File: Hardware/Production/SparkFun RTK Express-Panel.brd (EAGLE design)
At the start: 219.3 x 141.9 mm, 495 parts, among them J13 Internal, J16 microSD, J17 Qwiic Right Angle, J19 External, J21 USB Female Type C Connector, J24 USB Female Type C Connector, J3 USB Female Type C Connector, J31 microSD, J33 Qwiic Right Angle, J34 Internal, J39 External, J4 External, J40 USB Female Type C Connector, J43 USB Female Type C Connector, J5 USB Female Type C Connector, J50 microSD, J52 Qwiic Right Angle, J53 Internal, Q1 SIL2308-TP, Q2 MBT3904DW1T1, Q3 MBT3904DW1T1, Q4 SIL2308-TP, Q5 MBT3904DW1T1, Q6 SIL2308-TP, U1 74HC4052D, U10 MCP73833, U11 CH340C, U12 MAX17048, U13 LIS2DH12, U14 STLQ015-3.3V, U15 MCP73833, U16 74HC4052D, U17 LIS2DH12, U18 ESP-WROOM-3232D-NARROW, U19 AP2112K-3.3, U2 AP2112K-3.3, U20 U-BLOX_ZED-F9P, U21 CH340C, U22 MAX17048, U23 STLQ015-3.3V, U24 MCP73833, U25 74HC4052D, U26 LIS2DH12, U27 ESP-WROOM-3232D-NARROW, U3 U-BLOX_ZED-F9P, U4 STLQ015-3.3V, U5 ESP-WROOM-3232D-NARROW, U6 CH340C, U7 MAX17048, U8 AP2112K-3.3, U9 U-BLOX_ZED-F9P

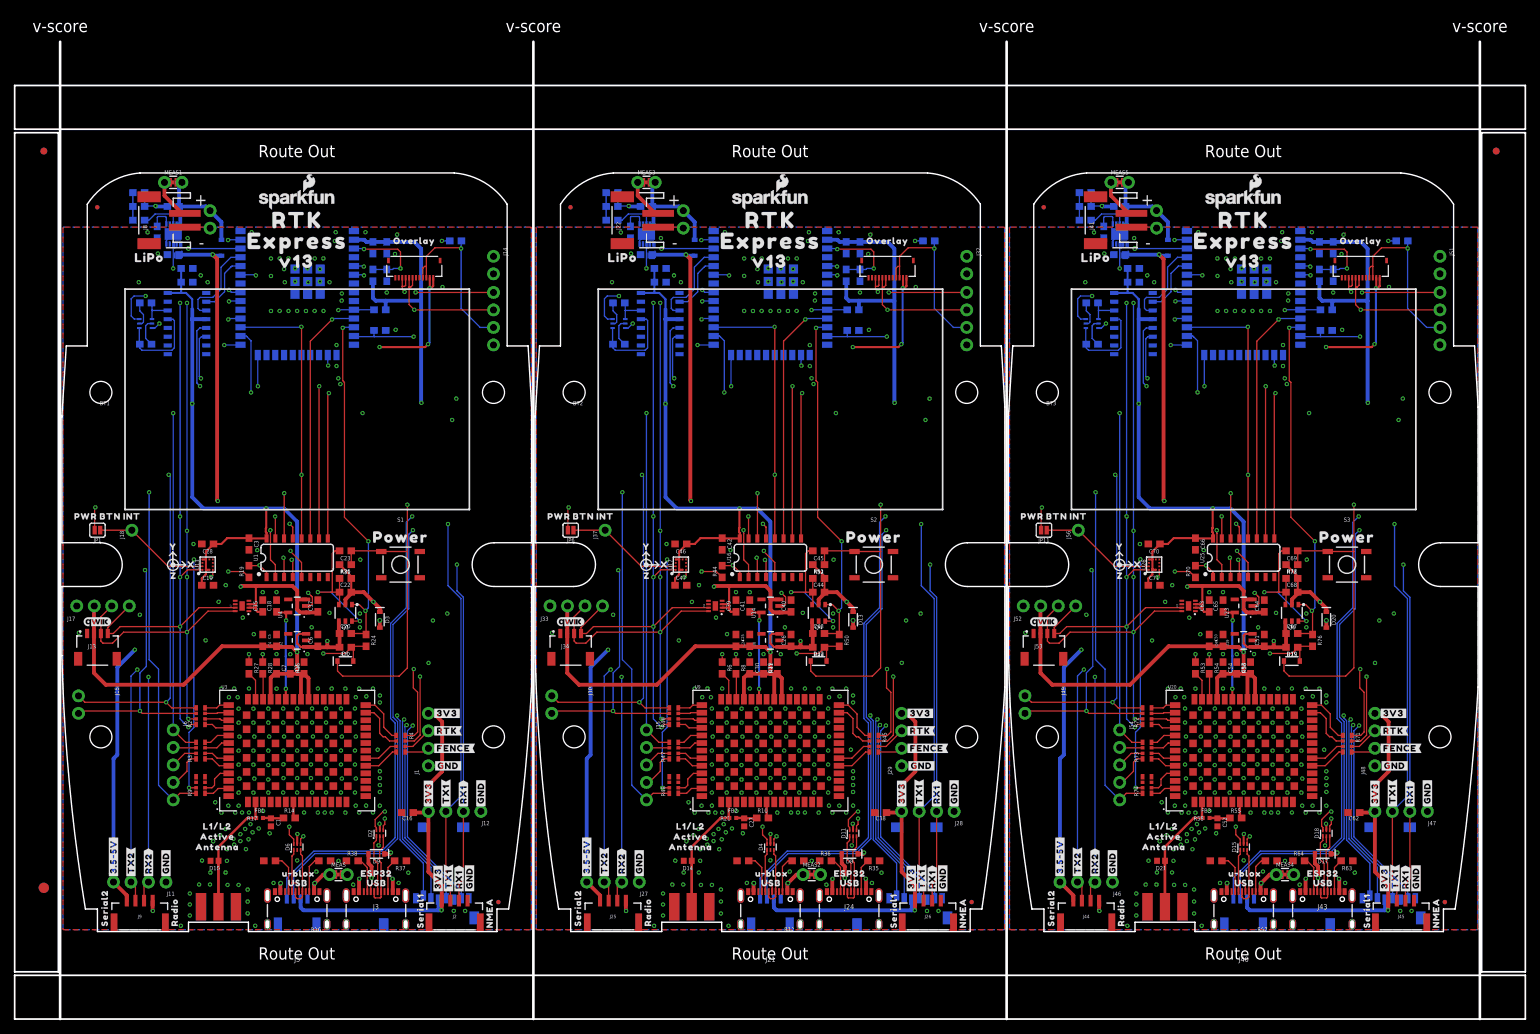
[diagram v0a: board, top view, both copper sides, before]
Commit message: Remove post mux opto isolation. Create v10 panel.
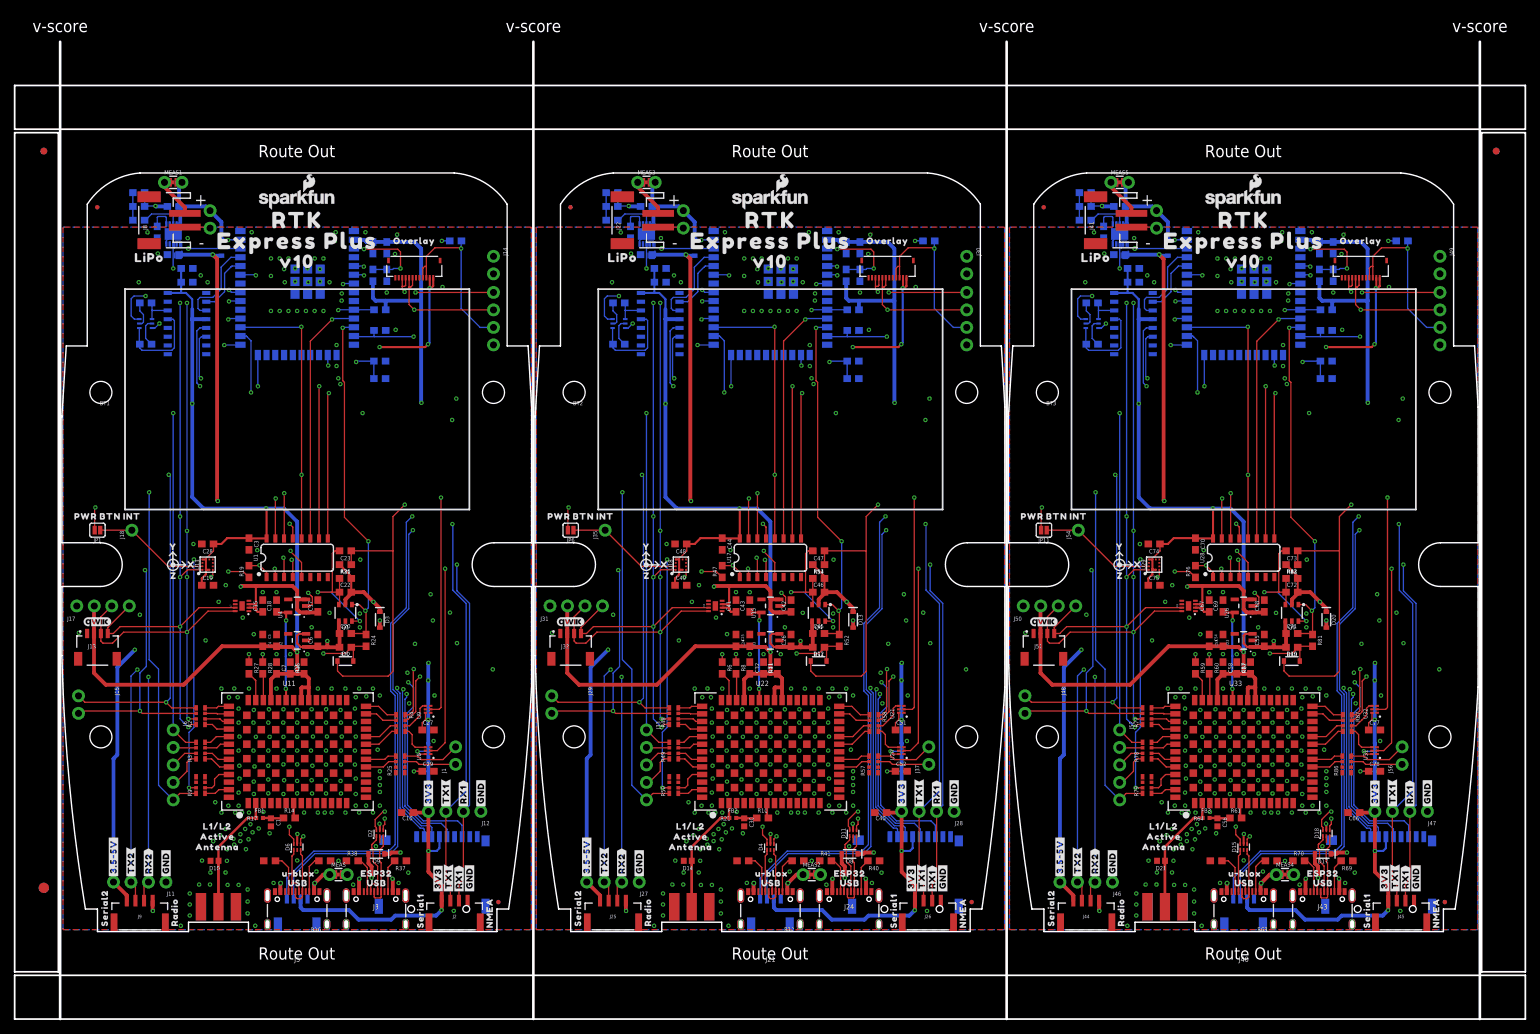
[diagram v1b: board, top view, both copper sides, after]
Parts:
- removed S1, S2, S3: Power, SparkFun-Switches:TACTILE_SWITCH_SMD_5.2MM
- removed U$181: (no value), output:PWR_BTN1
- removed U$182: (no value), output:OVERLAY0
- removed U$183: (no value), output:L1#L20
- removed U$184: (no value), output:ACTIVE1
- removed U$185: (no value), output:ANTENNA2
- removed U$186: (no value), output:V130
- added C73, C74, C76, C77, C78: 0.1uF, SparkFun-Capacitors:0603
- added C75: 10uF, SparkFun-Capacitors:0603
- added R79, R86, R87: 33, SparkFun-Resistors:1206_RA
- added R80, R82: 100k, SparkFun-Resistors:0603
- added R81: 300k, SparkFun-Resistors:0603
- added R83, R84: 10k, SparkFun-Resistors:0603
- added R85: 3.3k, SparkFun-Resistors:0603
- added U28: 74HC4052D, SparkFun-IC-Logic:SO16
- added U29: LIS2DH12, SparkFun-Sensors:LGA-12-LISDH12
- added U30: ESP-WROOM-3232D-NARROW, SparkFun-RF:ESP-WROOM-32D-NARROW
- added U31, U32: NC7SZ14-D, SparkFun-IC-Amplifiers:SIP6
- added U33: U-BLOX_ZED_F9R, SparkFun-GPS:UBLOX_ZED_F9R
- C27, C52: value 47pF -> 0.1uF; device SparkFun-Capacitors:0402 -> SparkFun-Capacitors:0603
- C29, C40, C41, C51, C64: value 1.0uF -> 0.1uF
- C30: value 0.1uF -> 47pF; device SparkFun-Capacitors:0603 -> SparkFun-Capacitors:0402
- C31, C55: value 4.7uF -> 1.0uF
- C32: value 4.7uF -> 0.1uF
- C33: value 10uF -> 4.7uF
- C34, C59, C60: value 0.1uF -> 4.7uF
- C35, C39, C45: value 0.1uF -> 10uF
- C37, C47, C67: value 10uF -> 0.1uF
- C42, C68, C69: value 0.1uF -> 1.0uF
- C43, C57: value 10uF -> 1.0uF
- C49, C65: value 1.0uF -> 10uF
- C56: value 4.7uF -> 47pF; device SparkFun-Capacitors:0603 -> SparkFun-Capacitors:0402
- J1, J29, J48: device SparkFun-Connectors:1X04_NO_SILK -> SparkFun-Connectors:1X02_NO_SILK
- J16: value microSD -> MICRO-SD-PUSH-PUSH-EXT-PIN; device SparkFun-Connectors:MICRO-SD-SOCKET -> SparkFun-Connectors:MICROSD-EXTERNALPIN
- J31, J50: value microSD -> Qwiic Right Angle; device SparkFun-Connectors:MICRO-SD-SOCKET -> SparkFun-Connectors:1X04_NO_SILK
- J32, J51: value (none) -> Internal; device SparkFun-Connectors:1X02_NO_SILK -> SparkFun-Connectors:JST04_1MM_RA
- J33, J52: value Qwiic Right Angle -> (none); device SparkFun-Connectors:1X04_NO_SILK -> SparkFun-Connectors:1X05_NO_SILK
- J34, J53: value Internal -> (none); device SparkFun-Connectors:JST04_1MM_RA -> SparkFun-Connectors:1X04_NO_SILK
- J35, J54: device SparkFun-Connectors:1X05_NO_SILK -> SparkFun-Connectors:1X01_NO_SILK
- J36, J55: device SparkFun-Connectors:1X04_NO_SILK -> RTK Facet:FPC_12_DOUBLESIDED_BACKFLIP
- J37, J56: device SparkFun-Connectors:1X01_NO_SILK -> SparkFun-Connectors:1X02_NO_SILK
- J38, J57: value (none) -> MICRO-SD-PUSH-PUSH-EXT-PIN; device RTK Facet:FPC_12_DOUBLESIDED_BACKFLIP -> SparkFun-Connectors:MICROSD-EXTERNALPIN
- R25: value 1k -> 33; device SparkFun-Resistors:0603 -> SparkFun-Resistors:1206_RA
- R32, R65: value 100k -> 1k
- R34: value 10k -> 3.3k
- R35: value 5.1k -> 100k
- R36: value 5.1k -> 10k
- R39, R75: value 100k -> 10k
- R40: value 470 -> 5.1k
- R41: value 150k -> 5.1k
- R42: value 0 -> 100k
- R43: value 10k -> 470
- R44: value 1k -> 150k
- R45, R74: value 33 -> 0; device SparkFun-Resistors:1206_RA -> SparkFun-Resistors:0603
- R46: value 33 -> 10k; device SparkFun-Resistors:1206_RA -> SparkFun-Resistors:0603
- R47: value 33 -> 1k; device SparkFun-Resistors:1206_RA -> SparkFun-Resistors:0603
- R49, R77: value 100k -> 33; device SparkFun-Resistors:0603 -> SparkFun-Resistors:1206_RA
- R50: value 300k -> 33; device SparkFun-Resistors:0603 -> SparkFun-Resistors:1206_RA
- R52: value 10k -> 300k
- R53: value 27 -> 100k
- R54: value 27 -> 10k
- R55: value 10 -> 10k
- R56: value 100k -> 3.3k
- R57, R58: value 5.1k -> 33; device SparkFun-Resistors:0603 -> SparkFun-Resistors:1206_RA
- R59: value 1k -> 27
- R60: value 100k -> 27
- R61: value 10k -> 10
- R62: value 10k -> 100k
- R66: value 470 -> 100k
- R67: value 150k -> 10k
- R68: value 0 -> 10k
- R69: value 10k -> 5.1k
- R70: value 1k -> 5.1k
- R71: value 33 -> 100k; device SparkFun-Resistors:1206_RA -> SparkFun-Resistors:0603
- R72: value 33 -> 470; device SparkFun-Resistors:1206_RA -> SparkFun-Resistors:0603
- R73: value 33 -> 150k; device SparkFun-Resistors:1206_RA -> SparkFun-Resistors:0603
- R76: value 300k -> 1k
- R78: value 10k -> 33; device SparkFun-Resistors:0603 -> SparkFun-Resistors:1206_RA
- U$1: device output:#GND#0 -> SparkFun-Aesthetics:QWIIC_4MM
- U$100: device output:RTK0 -> output:#SDA#0
- U$101: device output:#GND#2 -> output:#D_SEL#0
- U$102: device output:#3V3#2 -> SparkFun-Aesthetics:QWIIC_4MM
- U$103: device output:#SCL#1 -> output:#TX_RDY#0
- U$104: device output:#SDA#0 -> output:CHG2
- U$105: device output:#D_SEL#0 -> output:GND3
- U$106: device SparkFun-Aesthetics:QWIIC_4MM -> output:PWR0
- U$107: device output:#TX_RDY#0 -> output:SETUP1
- U$108: device output:POWER0 -> output:X0
- U$109: device output:CHG2 -> output:Y1
- U$110: device output:GND3 -> output:Z2
- U$111: device output:PWR0 -> output:INT0
- U$112: device output:SETUP1 -> output:PWR_BTN1
- U$113: device output:EXPRESS0 -> output:OVERLAY0
- U$114: device output:EXPRESS0 -> output:L1#L20
- U$115: device output:X0 -> output:ACTIVE1
- U$116: device output:Y1 -> output:ANTENNA2
- U$117: device output:Z2 -> output:V100
- U$118: device output:INT0 -> output:V100
- U$119: device output:PWR_BTN1 -> output:EXPRESS_PLUS0
- U$12: device output:#3V3#0 -> output:EXPRESS_PLUS0
- U$120: device output:OVERLAY0 -> output:EXPRESS_PLUS0
- U$121: device output:L1#L20 -> SparkFun-Aesthetics:QWIIC_4MM
- U$122: device output:ACTIVE1 -> output:#RTK#1
- U$123: device output:ANTENNA2 -> SparkFun GPS RTK Surveyor:1553DBK-ENCLOSURE
- U$124: device output:V130 -> output:LIPO0
- U$125: device SparkFun-Aesthetics:QWIIC_4MM -> output:U#BLOX0
- U$126: device output:#3V3#0 -> output:USB1
- U$127: device output:#GND#0 -> output:SERIAL20
- U$128: device output:#RTK#1 -> output:SERIAL10
- U$129: device SparkFun GPS RTK Surveyor:1553DBK-ENCLOSURE -> output:#RX2#2
- U$130: device output:LIPO0 -> output:#TX2#1
- U$131: device output:U#BLOX0 -> output:#RX1#2
- U$132: device output:USB1 -> output:#TX1#1
- U$133: device output:SERIAL20 -> output:#3V3#0
- U$134: device output:SERIAL10 -> output:#GND#0
- U$135: device output:#RX2#2 -> output:#GND#0
- U$136: device output:#TX2#1 -> output:NMEA1
- U$137: device output:#RX1#2 -> output:RADIO0
- U$138: device output:#TX1#1 -> output:##RST##4
- U$139: device output:#3V3#0 -> output:##SAFE##5
- U$140: device output:#GND#0 -> output:#FENCE#3
- U$141: device output:#GND#0 -> output:#3#5#5V#0
- U$142: device output:NMEA1 -> output:#PPS#0
- U$143: device output:RADIO0 -> output:#RX#2
- U$144: device output:##RST##4 -> output:ZED0
- U$145: device output:##SAFE##5 -> output:#TX#1
- U$146: device output:#FENCE#3 -> output:USB1
- U$147: device output:#3#5#5V#0 -> output:ESP320
- U$148: device output:#PPS#0 -> output:#3V3#0
- U$149: device output:#RX#2 -> output:#TX1#1
- U$150: device output:ZED0 -> output:#RX1#2
- U$151: device output:#TX#1 -> output:#GND#0
- U$152: device output:USB1 -> output:MICROSD0
- U$153: device output:ESP320 -> output:#GND#1
- U$154: device output:#3V3#0 -> output:#ESP_RST#0
- U$155: device output:#TX1#1 -> output:RTK0
- U$156: device output:#RX1#2 -> output:RTK0
- U$157: device output:#GND#0 -> output:#GND#2
- U$158: device output:MICROSD0 -> output:#3V3#2
- U$159: device output:#GND#1 -> output:#SCL#1
- U$160: device output:#ESP_RST#0 -> output:#SDA#0
- U$161: device output:RTK0 -> output:#D_SEL#0
- U$162: device output:RTK0 -> SparkFun-Aesthetics:QWIIC_4MM
- U$163: device output:#GND#2 -> output:#TX_RDY#0
- U$164: device output:#3V3#2 -> output:CHG2
- U$165: device output:#SCL#1 -> output:GND3
- U$166: device output:#SDA#0 -> output:PWR0
- U$167: device output:#D_SEL#0 -> output:SETUP1
- U$168: device SparkFun-Aesthetics:QWIIC_4MM -> output:X0
- U$169: device output:#TX_RDY#0 -> output:Y1
- U$170: device output:POWER0 -> output:Z2
- U$171: device output:CHG2 -> output:INT0
- U$172: device output:GND3 -> output:PWR_BTN1
- U$173: device output:PWR0 -> output:OVERLAY0
- U$174: device output:SETUP1 -> output:L1#L20
- U$175: device output:EXPRESS0 -> output:ACTIVE1
- U$176: device output:EXPRESS0 -> output:ANTENNA2
- U$177: device output:X0 -> output:V100
- U$178: device output:Y1 -> output:V100
- U$179: device output:Z2 -> output:EXPRESS_PLUS0
- U$18: device output:V130 -> SparkFun GPS RTK Surveyor:1553DBK-ENCLOSURE
- U$180: device output:INT0 -> output:EXPRESS_PLUS0
- U$19: device output:#GND#0 -> output:LIPO0
- U$2: device SparkFun-Aesthetics:QWIIC_4MM -> output:#RTK#1
- U$20: device output:#RTK#1 -> output:V100
- U$21: device SparkFun GPS RTK Surveyor:1553DBK-ENCLOSURE -> output:V100
- U$22: device output:LIPO0 -> output:EXPRESS_PLUS0
- U$31: device output:POWER0 -> output:USB1
- U$37: device output:#3V3#0 -> output:SERIAL20
- U$44: device output:USB1 -> output:SERIAL10
- U$51: device output:EXPRESS0 -> output:#RX2#2
- U$52: device output:SERIAL20 -> output:#TX2#1
- U$53: device output:EXPRESS0 -> output:#RX1#2
- U$54: device output:SERIAL10 -> output:#TX1#1
- U$57: device output:#RX2#2 -> output:#3V3#0
- U$58: device output:#TX2#1 -> output:#GND#0
- U$59: device output:#RX1#2 -> output:#GND#0
- U$61: device output:#TX1#1 -> output:NMEA1
- U$62: device output:#3V3#0 -> output:RADIO0
- U$63: device output:#GND#0 -> output:##RST##4
- U$64: device output:#GND#0 -> output:##SAFE##5
- U$69: device output:NMEA1 -> output:#FENCE#3
- U$71: device output:RADIO0 -> output:#3#5#5V#0
- U$73: device output:##RST##4 -> output:#PPS#0
- U$75: device output:##SAFE##5 -> output:#RX#2
- U$76: device output:#FENCE#3 -> output:ZED0
- U$77: device output:#3#5#5V#0 -> output:#TX#1
- U$78: device output:#PPS#0 -> output:USB1
- U$79: device output:#RX#2 -> output:ESP320
- U$80: device output:ZED0 -> output:#3V3#0
- U$81: device output:#TX#1 -> output:#TX1#1
- U$89: device output:USB1 -> output:#RX1#2
- U$90: device output:ESP320 -> output:#GND#0
- U$91: device output:#3V3#0 -> output:MICROSD0
- U$92: device output:#TX1#1 -> output:#GND#1
- U$94: device output:#RX1#2 -> output:#ESP_RST#0
- U$95: device output:#GND#0 -> output:RTK0
- U$96: device output:MICROSD0 -> output:RTK0
- U$97: device output:#GND#1 -> output:#GND#2
- U$98: device output:#ESP_RST#0 -> output:#3V3#2
- U$99: device output:RTK0 -> output:#SCL#1
- U11: value CH340C -> U-BLOX_ZED_F9R; device SparkFun-IC-Comms:SO016 -> SparkFun-GPS:UBLOX_ZED_F9R
- U12: value MAX17048 -> CH340C; device SparkFun-IC-Power:DFN-8 -> SparkFun-IC-Comms:SO016
- U14: value STLQ015-3.3V -> MAX17048; device SparkFun-IC-Power:SOT23-5 -> SparkFun-IC-Power:DFN-8
- U15: value MCP73833 -> STLQ015-3.3V; device SparkFun-IC-Power:DFN-10 -> SparkFun-IC-Power:SOT23-5
- U16: value 74HC4052D -> MCP73833; device SparkFun-IC-Logic:SO16 -> SparkFun-IC-Power:DFN-10
- U17: value LIS2DH12 -> 74HC4052D; device SparkFun-Sensors:LGA-12-LISDH12 -> SparkFun-IC-Logic:SO16
- U18: value ESP-WROOM-3232D-NARROW -> LIS2DH12; device SparkFun-RF:ESP-WROOM-32D-NARROW -> SparkFun-Sensors:LGA-12-LISDH12
- U19: value AP2112K-3.3 -> ESP-WROOM-3232D-NARROW; device SparkFun-IC-Power:SOT23-5 -> SparkFun-RF:ESP-WROOM-32D-NARROW
- U20, U9: value U-BLOX_ZED-F9P -> NC7SZ14-D; device SparkFun-GPS:ZED-F9P -> SparkFun-IC-Amplifiers:SIP6
- U21: value CH340C -> NC7SZ14-D; device SparkFun-IC-Comms:SO016 -> SparkFun-IC-Amplifiers:SIP6
- U22: value MAX17048 -> U-BLOX_ZED_F9R; device SparkFun-IC-Power:DFN-8 -> SparkFun-GPS:UBLOX_ZED_F9R
- U23: value STLQ015-3.3V -> AP2112K-3.3
- U24: value MCP73833 -> CH340C; device SparkFun-IC-Power:DFN-10 -> SparkFun-IC-Comms:SO016
- U25: value 74HC4052D -> MAX17048; device SparkFun-IC-Logic:SO16 -> SparkFun-IC-Power:DFN-8
- U26: value LIS2DH12 -> STLQ015-3.3V; device SparkFun-Sensors:LGA-12-LISDH12 -> SparkFun-IC-Power:SOT23-5
- U27: value ESP-WROOM-3232D-NARROW -> MCP73833; device SparkFun-RF:ESP-WROOM-32D-NARROW -> SparkFun-IC-Power:DFN-10
- U3: value U-BLOX_ZED-F9P -> AP2112K-3.3; device SparkFun-GPS:ZED-F9P -> SparkFun-IC-Power:SOT23-5
- U8: value AP2112K-3.3 -> NC7SZ14-D; device SparkFun-IC-Power:SOT23-5 -> SparkFun-IC-Amplifiers:SIP6
- moved U$20 111.5 mm to (34.2, 97.3)
- moved R69 104.2 mm to (186.6, 10.3), flipped to the top, turned to 180 degrees
- moved U$51 103.9 mm to (81.3, 7.70), turned to 90 degrees
- moved U$122 103.7 mm to (194.1, 26.8), flipped to the bottom
- moved U$53 102.5 mm to (126.4, 5.51), flipped to the top, turned to 90 degrees
- moved R41 99.9 mm to (110.9, 10.3), flipped to the top
- moved J38 93.0 mm to (122.5, 3.27), flipped to the bottom, turned to 0 degrees
- moved J57 93.0 mm to (191.2, 3.27), flipped to the bottom, turned to 0 degrees
- moved R40 90.4 mm to (117.9, 10.3), flipped to the top, turned to 180 degrees
- moved U$12 90.2 mm to (34.2, 50.3), flipped to the bottom
- moved U$130 90.2 mm to (147.4, 7.70), turned to 90 degrees
- moved U$123 90.2 mm to (171.6, 53.3), turned to 90 degrees
- moved U$95 89.5 mm to (102.9, 103.3), turned to 0 degrees
- moved U$153 89.2 mm to (199.5, 95.4), flipped to the bottom
- moved U$155 88.1 mm to (171.6, 103.3), turned to 0 degrees
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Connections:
- removed net ESP_I3: U27.4
- removed net ESP_I35: U5.7
- removed net ESP_I4: U27.7
- removed net N$14 (its old number): R42.1, U15.8
- removed net N$16 (its old number): R44.1, U18.28
- removed net N$29 (its old number): C68.1, C69.2, Q6.D1, Q6.G2, R77.1
- removed net PPS: R9.P1, U3.53
- removed net PPS1: R48.P1, U9.53
- removed net PPS2: R74.P1, U20.53
- removed net RTK_LV: R4.P3, U3.20
- removed net RTK_LV1: R45.P3, U9.20
- removed net RTK_LV2: R71.P3, U20.20
- new net ESP_3V1: R56.2
- new net ESP_3V2: R85.2
- new net ESP_3V3: R34.2
- new net ESP_I35/DEVICE_SENSE: R33.2, R34.1, U5.7
- new net ESP_I35/DEVICE_SENSE1: R55.2, R56.1, U19.7
- new net ESP_I35/DEVICE_SENSE2: R84.2, R85.1, U30.7
- new net EXT_DIR: U1.15, U9.P2
- new net EXT_DIR1: U17.15, U21.P2
- new net EXT_DIR2: U28.15, U32.P2
- new net EXT_WT: U1.2, U8.P2
- new net EXT_WT1: U17.2, U20.P2
- new net EXT_WT2: U28.2, U31.P2
- new net N$10: Q3.2, R39.2
- new net N$23: R60.2, U33.P39
- new net N$26: R61.2, U33.P7
- new net N$31: R74.1, U27.8
- new net N$33: R76.1, U30.28
- new net N$34: C72.1, C73.2, Q6.D1, Q6.G2, R82.1
- new net N$35: R87.P4, U33.P22
- new net N$36: R87.P3, U33.P23
- new net N$9: Q3.5, R36.2
- new net PPS_LV: R9.P1, U11.P53
- new net PPS_LV1: R50.P1, U22.P53
- new net PPS_LV2: R79.P1, U33.P53
- new net RTK_STAT_LV: R25.P5, U11.P20
- new net RTK_STAT_LV1: R57.P5, U22.P20
- new net RTK_STAT_LV2: R86.P5, U33.P20
- new net ZED_DIR: R4.P6, U9.P4
- new net ZED_DIR1: R58.P6, U21.P4
- new net ZED_DIR2: R87.P6, U32.P4
- new net ZED_WT: R4.P5, U8.P4
- new net ZED_WT1: R58.P5, U20.P4
- new net ZED_WT2: R87.P5, U31.P4
- net 3.3V: now also C27.1, C29.1, J16.4, U11.P33, U11.P34, U11.P38, U8.P6, U9.P6; no longer J1.4, J16.VCC, U3.33, U3.34, U3.38
- net 3.3V1: now also C31.1, C32.2, C35.1, C39.1, C40.1, C44.1, C48.1, C49.1, C51.1, C52.1, J31.2, J32.2, J38.4, R35.2, R42.2, U12.16, U12.4, U17.16, U18.10, U18.3, U18.9, U19.2, U20.P6, U21.P6, U22.P33, U22.P34, U22.P38, U3.5; no longer C29.1, C30.2, C33.1, C34.1, C37.1, C42.1, C46.1, C47.1, J29.4, J31.VCC, J33.2, J34.2, R32.2, R39.2, U11.16, U11.4, U16.16, U17.10, U17.2, U17.3, U17.9, U8.5, U9.33, U9.34, U9.38
- net 3.3V2: now also C58.2, C64.1, C65.1, C74.1, C75.1, C77.1, C78.1, J50.2, J51.2, J57.4, R62.2, R66.2, R71.2, U23.5, U24.16, U24.4, U28.16, U29.10, U29.2, U29.3, U29.9, U30.2, U31.P6, U32.P6, U33.P33, U33.P34, U33.P38; no longer C49.1, C50.2, C58.1, C60.1, C71.1, J48.4, J50.VCC, J52.2, J53.2, R56.2, R60.2, R65.2, U19.5, U20.33, U20.34, U20.38, U21.16, U21.4, U25.16, U26.10, U26.2, U26.3, U26.9, U27.2
- net ANT_VCC1: now also C30.1; no longer C27.1
- net ANT_VCC2: now also C56.1, R61.1; no longer C52.1, R55.1
- net CC10: now also R63.2; no longer R57.2
- net CC11: now also R69.2; no longer R63.2
- net CC12: now also R70.2; no longer R64.2
- net CC7: now also R40.2; no longer R35.2
- net CC8: now also R41.2; no longer R36.2
- net CC9: now also R64.2; no longer R58.2
- net CHG_LED1: now also R43.2, U16.3; no longer R40.2, U15.3
- net CHG_LED2: now also R72.2, U27.3; no longer R66.2, U24.3
- net CHG_LED_RES1: now also J34.2, J36.3, J36.4, R43.1; no longer J36.2, J38.3, J38.4, R40.1
- net CHG_LED_RES2: now also J53.2, J55.3, J55.4, R72.1; no longer J55.2, J57.3, J57.4, R66.1
- net CHG_THERM2: now also R44.2, R45.2, R46.2; no longer R41.2, R42.2, R43.2
- net CHG_THERM3: now also R73.2, R74.2, R75.2; no longer R67.2, R68.2, R69.2
- net D+3: now also U12.5; no longer U11.5
- net D+4: now also R59.1; no longer R53.1
- net D+5: now also U24.5; no longer U21.5
- net D-3: now also U12.6; no longer U11.6
- net D-4: now also R60.1; no longer R54.1
- net D-5: now also U24.6; no longer U21.6
- net ESP32_!DTR1: now also R36.1, U12.13; no longer R33.1, U11.13
- net ESP32_!DTR2: now also R67.1, U24.13; no longer R61.1, U21.13
- net ESP32_!RTS1: now also R39.1, U12.14; no longer R34.1, U11.14
- net ESP32_!RTS2: now also R68.1, U24.14; no longer R62.1, U21.14
- net ESP32_EN1: now also C37.1, J30.1, R35.1, U19.3; no longer C35.1, J32.1, R32.1, U18.3
- net ESP32_EN2: now also C63.1, J49.1, R66.1, U30.3; no longer C59.1, J51.1, R60.1, U27.3
- net ESP32_RXI1: now also U12.2, U19.34; no longer U11.2, U18.34
- net ESP32_RXI2: now also U24.2, U30.34; no longer U21.2, U27.34
- net ESP32_TXO1: now also U12.3, U19.35; no longer U11.3, U18.35
- net ESP32_TXO2: now also U24.3, U30.35; no longer U21.3, U27.35
- net ESP_0/BOOT1: now also U19.25; no longer U18.25
- net ESP_0/BOOT2: now also U30.25; no longer U27.25
- net ESP_1: now also U19.29; no longer U18.29
- net ESP_10: now also U30.9; no longer U27.9
- net ESP_11: now also U30.8; no longer U27.8
- net ESP_13/POWER_CTRL1: now also R51.1, R52.2, U19.16; no longer R49.1, R50.2, U18.16
- net ESP_13/POWER_CTRL2: now also R80.1, R81.2, U30.16; no longer R75.1, R76.2, U27.16
- net ESP_14/SETUP_BUTTON1: now also C50.1, J34.3, J36.7, J36.8, U19.13; no longer C48.1, J36.3, J38.7, J38.8, U18.13
- net ESP_14/SETUP_BUTTON2: now also C76.1, J53.3, J55.7, J55.8, U30.13; no longer C72.1, J55.3, J57.7, J57.8, U27.13
- net ESP_18/SCK: now also J16.5; no longer J16.SCLK
- net ESP_18/SCK1: now also J38.5, U19.30; no longer J31.SCLK, U18.30
- net ESP_18/SCK2: now also J57.5, U30.30; no longer J50.SCLK, U27.30
- net ESP_19/CIPO: now also J16.7; no longer J16.DO/DAT0
- net ESP_19/CIPO1: now also J38.7, U19.31; no longer J31.DO/DAT0, U18.31
- net ESP_19/CIPO2: now also J57.7, U30.31; no longer J50.DO/DAT0, U27.31
- net ESP_2: now also U19.14; no longer U18.14
- net ESP_2/MUX_A1: now also U17.10, U19.24; no longer U16.10, U18.24
- net ESP_2/MUX_A2: now also U28.10, U30.24; no longer U25.10, U27.24
- net ESP_21/SDA: no longer U1.2
- net ESP_21/SDA1: now also J31.3, J32.3, R48.P7, U14.8, U18.4, U19.33; no longer J33.3, J34.3, R46.P7, U12.8, U16.2, U17.4, U18.33
- net ESP_21/SDA2: now also J50.3, J51.3, R77.P7, U25.8, U29.4, U30.33; no longer J52.3, J53.3, R72.P7, U22.8, U25.2, U26.4, U27.33
- net ESP_22/SCL: no longer U1.15
- net ESP_22/SCL1: now also J31.4, J32.4, R48.P8, U14.7, U18.1, U19.36; no longer J33.4, J34.4, R46.P8, U12.7, U16.15, U17.1, U18.36
- net ESP_22/SCL2: now also J50.4, J51.4, R77.P8, U25.7, U29.1, U30.36; no longer J52.4, J53.4, R72.P8, U22.7, U25.15, U26.1, U27.36
- net ESP_23/COPI: now also J16.3; no longer J16.DI/CMD
- net ESP_23/COPI1: now also J38.3, U19.37; no longer J31.DI/CMD, U18.37
- net ESP_23/COPI2: now also J57.3, U30.37; no longer J50.DI/CMD, U27.37
- net ESP_25/SD_!CS!: now also J16.2; no longer J16.CS/DAT3
- net ESP_25/SD_!CS!1: now also J38.2, R42.1, U19.10; no longer J31.CS/DAT3, R39.1, U18.10
- net ESP_25/SD_!CS!2: now also J57.2, R71.1, U30.10; no longer J50.CS/DAT3, R65.1, U27.10
- net ESP_26/DAC1: now also U17.11, U19.11; no longer U16.11, U18.11
- net ESP_26/DAC3: now also U28.11, U30.11; no longer U25.11, U27.11
- net ESP_26/ZED_TX_READY_LV: now also U11.P46; no longer U3.46
- net ESP_26/ZED_TX_READY_LV1: now also R49.P4, U22.P46; no longer R47.P4, U9.46
- net ESP_26/ZED_TX_READY_LV2: now also R78.P4, U33.P46; no longer R73.P4, U20.46
- net ESP_27/FAST_OFF1: now also C45.2, R52.1, U19.12; no longer C43.2, R50.1, U18.12
- net ESP_27/FAST_OFF2: now also C71.2, R81.1, U30.12; no longer C67.2, R76.1, U27.12
- net ESP_3: now also U19.23; no longer U18.23
- net ESP_4: now also U19.9; no longer U18.9
- net ESP_4/ACCEL_INT1: now also J35.1, U18.12; no longer J37.1, U17.12
- net ESP_4/ACCEL_INT2: now also J54.1, U29.12; no longer J56.1, U26.12
- net ESP_4/MUX_B1: now also U17.9, U19.26; no longer U16.9, U18.26
- net ESP_4/MUX_B2: now also U28.9, U30.26; no longer U25.9, U27.26
- net ESP_6: now also U19.8; no longer U18.8
- net ESP_7: now also U30.29; no longer U27.29
- net ESP_8: now also U30.14; no longer U27.14
- net ESP_9: now also U30.23; no longer U27.23
- net ESP_I1: now also U19.4; no longer U18.4
- net ESP_I16/ZED-TXO2: now also J29.1, R48.P5, U17.12, U19.27; no longer J30.1, R46.P5, U16.12, U18.27
- net ESP_I16/ZED-TXO3: now also J48.1, R77.P5, U28.12, U30.27; no longer J49.1, R72.P5, U25.12, U27.27
- net ESP_I2: now also U30.4; no longer U18.7
- net ESP_I34/ZED_TX_READY1: now also J33.1, R49.P5, U19.6; no longer J35.1, R47.P5, U18.6
- net ESP_I34/ZED_TX_READY2: now also J52.1, R78.P5, U30.6; no longer J54.1, R73.P5, U27.6
- net ESP_I39/ADC1: now also U17.4, U19.5; no longer U16.4, U18.5
- net ESP_I39/ADC2: now also U28.4, U30.5; no longer U25.4, U27.5
- net ESP_O17/ZED-RXI2: now also J29.2, R47.2, R48.P6, U17.1; no longer J30.2, R44.2, R46.P6, U16.1
- net ESP_O17/ZED-RXI3: now also J48.2, R76.2, R77.P6, U28.1; no longer J49.2, R70.2, R72.P6, U25.1
- net EXTERNAL_DATA_IN1: now also U17.3; no longer U16.3
- net EXTERNAL_DATA_IN2: now also U28.3; no longer U25.3
- net EXTERNAL_DATA_OUT1: now also U17.13; no longer U16.13
- net EXTERNAL_DATA_OUT2: now also U28.13; no longer U25.13
- net EXTINT_LV: now also U11.P51; no longer U3.51
- net EXTINT_LV1: now also R50.P2, U22.P51; no longer R48.P2, U9.51
- net EXTINT_LV2: now also R79.P2, U33.P51; no longer R74.P2, U20.51
- net FENCE_LV: now also R25.P6, U11.P19; no longer R4.P4, U3.19
- net FENCE_LV1: now also R57.P6, U22.P19; no longer R45.P4, U9.19
- net FENCE_LV2: now also R86.P6, U33.P19; no longer R71.P4, U20.19
- net GND: now also C27.2, C29.2, J16.10, J16.11, J16.12, J16.13, J16.6, R33.1, U11.G1, U11.G10, U11.G11, U11.G12, U11.G13, U11.G14, U11.G15, U11.G16, U11.G17, U11.G18, U11.G19, U11.G2, U11.G20, U11.G21, U11.G22, U11.G23, U11.G24, U11.G25, U11.G26, U11.G27, U11.G28, U11.G29, U11.G3, U11.G30, U11.G31, U11.G32, U11.G33, U11.G34, U11.G35, U11.G36, U11.G37, U11.G38, U11.G39, U11.G4, U11.G40, U11.G41, U11.G42, U11.G43, U11.G44, U11.G45, U11.G46, U11.G47, U11.G48, U11.G5, U11.G6, U11.G7, U11.G8, U11.G9, U11.P1, U11.P12, U11.P14, U11.P3, U11.P32, U11.P37, U11.P41, U11.P48, U8.P3, U9.P3; no longer J1.1, J16.CD1, J16.GND, J16.GND1, J16.GND3, S1.3, U3.1, U3.100, U3.101, U3.102, U3.12, U3.14, U3.3, U3.32, U3.37, U3.41, U3.48, U3.55, U3.56, U3.57, U3.58, U3.59, U3.60, U3.61, U3.62, U3.63, U3.64, U3.65, U3.66, U3.67, U3.68, U3.69, U3.70, U3.71, U3.72, U3.73, U3.74, U3.75, U3.76, U3.77, U3.78, U3.79, U3.80, U3.81, U3.82, U3.83, U3.84, U3.85, U3.86, U3.87, U3.88, U3.89, U3.90, U3.91, U3.92, U3.93, U3.94, U3.95, U3.96, U3.97, U3.98, U3.99
- net GND1: now also C30.2, C32.1, C43.2, C44.2, C49.2, C50.2, C51.2, C52.2, J30.2, J31.1, J32.1, J36.11, J36.12, J38.10, J38.13, J38.6, R32.1, R40.1, R44.1, R46.1, R55.1, U14.1, U14.4, U14.6, U14.9, U15.2, U16.11, U16.5, U18.5, U18.6, U18.7, U18.8, U19.1, U19.15, U19.38, U19.GND1, U19.GNDT1, U19.GNDT2, U19.GNDT3, U19.GNDT4, U19.GNDT5, U19.GNDT6, U19.GNDT7, U19.GNDT8, U20.P3, U21.P3, U22.G1, U22.G10, U22.G11, U22.G12, U22.G13, U22.G14, U22.G15, U22.G16, U22.G17, U22.G18, U22.G19, U22.G2, U22.G20, U22.G21, U22.G22, U22.G23, U22.G24, U22.G25, U22.G26, U22.G27, U22.G28, U22.G29, U22.G3, U22.G30, U22.G31, U22.G32, U22.G33, U22.G34, U22.G35, U22.G36, U22.G37, U22.G38, U22.G39, U22.G4, U22.G40, U22.G41, U22.G42, U22.G43, U22.G44, U22.G45, U22.G46, U22.G47, U22.G48, U22.G5, U22.G6, U22.G7, U22.G8, U22.G9, U22.P1, U22.P12, U22.P14, U22.P3, U22.P32, U22.P37, U22.P41, U22.P48, U3.2; no longer C27.2, C29.2, C30.1, C32.2, C46.2, C47.2, J29.1, J31.CD1, J31.GND, J31.GND1, J31.GND3, J32.2, J33.1, J36.1, R25.1, R35.1, R36.1, R43.1, S2.3, U11.1, U12.4, U12.6, U12.9, U14.2, U15.11, U15.5, U16.6, U16.7, U16.8, U17.5, U18.1, U18.15, U18.38, U18.GND1, U18.GNDT1, U18.GNDT2, U18.GNDT3, U18.GNDT4, U18.GNDT5, U18.GNDT6, U18.GNDT7, U18.GNDT8, U8.2, U9.1, U9.100, U9.101, U9.102, U9.12, U9.14, U9.3, U9.32, U9.37, U9.41, U9.48, U9.55, U9.56, U9.57, U9.58, U9.59, U9.60, U9.61, U9.62, U9.63, U9.64, U9.65, U9.66, U9.67, U9.68, U9.69, U9.70, U9.71, U9.72, U9.73, U9.74, U9.75, U9.76, U9.77, U9.78, U9.79, U9.80, U9.81, U9.82, U9.83, U9.84, U9.85, U9.86, U9.87, U9.88, U9.89, U9.90, U9.91, U9.92, U9.93, U9.94, U9.95, U9.96, U9.97, U9.98, U9.99
- net GND2: now also C58.1, C67.2, C68.2, C69.2, C74.2, C75.2, C76.2, C77.2, C78.2, J49.2, J50.1, J51.1, J55.11, J55.12, J57.10, J57.13, J57.6, R62.1, R65.1, R70.1, R73.1, R75.1, R84.1, U24.1, U25.1, U25.4, U25.9, U26.2, U27.11, U27.5, U28.6, U28.7, U28.8, U29.5, U29.6, U29.7, U29.8, U30.1, U30.15, U30.38, U30.GND1, U30.GNDT1, U30.GNDT2, U30.GNDT3, U30.GNDT4, U30.GNDT5, U30.GNDT6, U30.GNDT7, U30.GNDT8, U31.P3, U32.P3, U33.G1, U33.G10, U33.G11, U33.G12, U33.G13, U33.G14, U33.G15, U33.G16, U33.G17, U33.G18, U33.G19, U33.G2, U33.G20, U33.G21, U33.G22, U33.G23, U33.G24, U33.G25, U33.G26, U33.G27, U33.G28, U33.G29, U33.G3, U33.G30, U33.G31, U33.G32, U33.G33, U33.G34, U33.G35, U33.G36, U33.G37, U33.G38, U33.G39, U33.G4, U33.G40, U33.G41, U33.G42, U33.G43, U33.G44, U33.G45, U33.G46, U33.G47, U33.G48, U33.G5, U33.G6, U33.G7, U33.G8, U33.G9, U33.P1, U33.P12, U33.P14, U33.P3, U33.P32, U33.P37, U33.P41, U33.P48; no longer C49.2, C50.1, C51.2, C52.2, C58.2, C71.2, C72.2, J48.1, J50.CD1, J50.GND, J50.GND1, J50.GND3, J51.2, J52.1, J55.1, R56.1, R57.1, R58.1, R59.1, R67.1, S3.3, U19.2, U20.1, U20.100, U20.101, U20.102, U20.12, U20.14, U20.3, U20.32, U20.37, U20.41, U20.48, U20.55, U20.56, U20.57, U20.58, U20.59, U20.60, U20.61, U20.62, U20.63, U20.64, U20.65, U20.66, U20.67, U20.68, U20.69, U20.70, U20.71, U20.72, U20.73, U20.74, U20.75, U20.76, U20.77, U20.78, U20.79, U20.80, U20.81, U20.82, U20.83, U20.84, U20.85, U20.86, U20.87, U20.88, U20.89, U20.90, U20.91, U20.92, U20.93, U20.94, U20.95, U20.96, U20.97, U20.98, U20.99, U21.1, U22.1, U22.4, U22.6, U22.9, U24.11, U24.5, U25.7, U25.8, U26.5, U26.6, U26.7, U26.8, U27.1, U27.15, U27.38, U27.GND1, U27.GNDT1, U27.GNDT2, U27.GNDT3, U27.GNDT4, U27.GNDT5, U27.GNDT6, U27.GNDT7, U27.GNDT8
- net GPS_ANT1: now also U11.P2; no longer U3.2
- net GPS_ANT2: now also U22.P2; no longer U9.2
- net GPS_ANT3: now also U33.P2; no longer U20.2
- net N$1: now also U22.P40; no longer U9.40
- net N$11: now also U11.P40; no longer U3.40
- net N$12: now also U11.P39; no longer U3.39
- net N$13: now also U11.P7; no longer U3.7
- net N$17: now also R45.1, U16.8; no longer C44.1, C45.2, Q4.D1, Q4.G2, R51.1
- net N$18: now also R47.1, U19.28; no longer R53.2, U20.40
- net N$19: now also C46.1, C47.2, Q4.D1, Q4.G2, R53.1; no longer R54.2, U20.39
- net N$2: now also R4.P4, U11.P22; no longer R8.2, U9.39
- net N$20: now also R58.P4, U22.P22; no longer R55.2, U20.7
- net N$21: now also R58.P3, U22.P23; no longer Q5.5, R61.2
- net N$22: now also R59.2, U33.P40; no longer Q5.2, R62.2
- net N$27: now also Q5.5, R67.2; no longer R68.1, U24.8
- net N$28: now also Q5.2, R68.2; no longer R70.1, U27.28
- net N$3: now also R4.P3, U11.P23; no longer R10.2, U9.7
- net N$7: now also R8.2, U22.P39; no longer Q3.5, R33.2
- net N$8: now also R10.2, U22.P7; no longer Q3.2, R34.2
- net POWER_BTN: no longer S1.1
- net POWER_BTN1: now also C47.1, J34.4, J36.10, J36.9, R54.1; no longer C45.1, J36.4, J38.10, J38.9, R52.1, S2.1
- net POWER_BTN2: now also C73.1, J53.4, J55.10, J55.9, R83.1; no longer C69.1, J55.4, J57.10, J57.9, R78.1, S3.1
- net PROG2: now also R32.2, U16.6; no longer R25.2, U15.6
- net PROG3: now also R65.2, U27.6; no longer R59.2, U24.6
- net RX2_LV: now also U11.P26; no longer U3.26
- net RX2_LV1: now also R58.P2, U22.P26; no longer R45.P2, U9.26
- net RX2_LV2: now also R87.P2, U33.P26; no longer R71.P2, U20.26
- net RXLV: now also U11.P43; no longer U3.43
- net RXLV1: now also R48.P3, U22.P43; no longer R46.P3, U9.43
- net RXLV2: now also R77.P3, U33.P43; no longer R72.P3, U20.43
- net SCL_LV: now also U11.P45; no longer U3.45
- net SCL_LV1: now also R48.P1, U22.P45; no longer R46.P1, U9.45
- net SCL_LV2: now also R77.P1, U33.P45; no longer R72.P1, U20.45
- net SDA_LV: now also U11.P44; no longer U3.44
- net SDA_LV1: now also R48.P2, U22.P44; no longer R46.P2, U9.44
- net SDA_LV2: now also R77.P2, U33.P44; no longer R72.P2, U20.44
- net TX2_LV: now also U11.P27; no longer U3.27
- net TX2_LV1: now also R58.P1, U22.P27; no longer R45.P1, U9.27
- net TX2_LV2: now also R87.P1, U33.P27; no longer R71.P1, U20.27
- net TXLV: now also U11.P42; no longer U3.42
- net TXLV1: now also R48.P4, U22.P42; no longer R46.P4, U9.42
- net TXLV2: now also R77.P4, U33.P42; no longer R72.P4, U20.42
- net VOUT1: now also C45.1, R51.2, U3.1, U3.3; no longer C43.1, R49.2, U8.1, U8.3
- net VOUT2: now also C55.1, C71.1, R80.2, U23.1, U23.3; no longer C51.1, C67.1, R75.2, U19.1, U19.3
- net V_BATT1: now also C33.1, C41.1, C42.1, U14.2, U15.1, U15.3, U16.10, U16.9; no longer C31.1, C39.1, C40.1, U12.2, U12.3, U14.1, U15.10, U15.9
- net V_BATT2: now also C59.1, C67.1, C68.1, U25.2, U25.3, U26.1, U26.3, U27.10, U27.9; no longer C55.1, C63.1, C64.1, U22.2, U22.3, U23.1, U23.3, U24.10, U24.9
- net V_BKCP: now also U11.P36; no longer U3.36
- net V_BKCP1: now also C43.1, U15.5, U22.P36; no longer C41.1, U14.5, U9.36
- net V_BKCP2: now also C69.1, U26.5, U33.P36; no longer C65.1, U20.36, U23.5
- net V_RAW1: now also C34.1, C46.2, R53.2, R54.2, U16.1, U16.2; no longer C32.1, C44.2, R51.2, R52.2, U15.1, U15.2
- net V_RAW2: now also C60.1, C72.2, R82.2, R83.2, U27.1, U27.2; no longer C56.1, C68.2, R77.2, R78.2, U24.1, U24.2
- net V_USB1: now also J36.1, J36.2; no longer J38.1, J38.2
- net V_USB2: now also J55.1, J55.2; no longer J57.1, J57.2
- net ZED-RXI1: now also R58.P7; no longer R45.P7
- net ZED-RXI3: now also R87.P7; no longer R71.P7
- net ZED-TXO1: now also R58.P8; no longer R45.P8
- net ZED-TXO3: now also R87.P8; no longer R71.P8
- net ZED_!RESET!1: now also J33.3, R49.P7; no longer J35.3, R47.P7
- net ZED_!RESET!2: now also J52.3, R78.P7; no longer J54.3, R73.P7
- net ZED_!RESET!_LV: now also U11.P49; no longer U3.49
- net ZED_!RESET!_LV1: now also R49.P2, U22.P49; no longer R47.P2, U9.49
- net ZED_!RESET!_LV2: now also R78.P2, U33.P49; no longer R73.P2, U20.49
- net ZED_!SAFE!1: now also J33.4, R49.P8; no longer J35.4, R47.P8
- net ZED_!SAFE!2: now also J52.4, R78.P8; no longer J54.4, R73.P8
- net ZED_!SAFE!_LV: now also U11.P50; no longer U3.50
- net ZED_!SAFE!_LV1: now also R49.P1, U22.P50; no longer R47.P1, U9.50
- net ZED_!SAFE!_LV2: now also R78.P1, U33.P50; no longer R73.P1, U20.50
- net ZED_D_SEL1: now also J33.2, R49.P6; no longer J35.2, R47.P6
- net ZED_D_SEL2: now also J52.2, R78.P6; no longer J54.2, R73.P6
- net ZED_D_SEL_LV: now also U11.P47; no longer U3.47
- net ZED_D_SEL_LV1: now also R49.P3, U22.P47; no longer R47.P3, U9.47
- net ZED_D_SEL_LV2: now also R78.P3, U33.P47; no longer R73.P3, U20.47
- net ZED_EXTINT1: now also R50.P7, U17.5; no longer R48.P7, U16.5
- net ZED_EXTINT2: now also R79.P7, U28.5; no longer R74.P7, U25.5
- net ZED_FENCE_STAT: now also J1.1, R25.P3; no longer J1.2, R4.P5
- net ZED_FENCE_STAT1: now also J37.1, R57.P3; no longer J29.2, R45.P5
- net ZED_FENCE_STAT2: now also J56.1, R86.P3; no longer J48.2, R71.P5
- net ZED_PPS_STAT1: now also J33.5, R50.P8, U17.14; no longer J35.5, R48.P8, U16.14
- net ZED_PPS_STAT2: now also J52.5, R79.P8, U28.14; no longer J54.5, R74.P8, U25.14
- net ZED_RTK_STAT: now also J1.2, R25.P4; no longer J1.3, R4.P6
- net ZED_RTK_STAT1: now also J37.2, R57.P4; no longer J29.3, R45.P6
- net ZED_RTK_STAT2: now also J56.2, R86.P4; no longer J48.3, R71.P6
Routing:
- net EXT_DIR2: track 0.00 -> 62.0 mm, vias 0 -> 2
- net EXT_DIR1: track 0.00 -> 62.0 mm, vias 0 -> 2
- net EXT_DIR: track 0.00 -> 62.0 mm, vias 0 -> 2
- net EXT_WT2: track 0.00 -> 53.8 mm, vias 0 -> 2
- net EXT_WT1: track 0.00 -> 53.8 mm, vias 0 -> 2
- net EXT_WT: track 0.00 -> 53.8 mm, vias 0 -> 2
- net N$33: track 0.00 -> 42.0 mm, vias 0 -> 2
- net N$16 (its old number): track 42.0 -> 0.00 mm, vias 2 -> 0
- net N$28: track 42.0 -> 3.70 mm, vias 2 -> 0
- net N$18: track 4.09 -> 42.0 mm, vias 0 -> 2
- net N$34: track 0.00 -> 22.9 mm, vias 0 -> 2
- net N$29 (its old number): track 22.9 -> 0.00 mm, vias 2 -> 0
- net N$19: track 3.72 -> 22.9 mm, vias 0 -> 2
- net ESP_I35/DEVICE_SENSE1: track 0.00 -> 18.9 mm, vias 0 -> 2
- net ESP_I35/DEVICE_SENSE: track 0.00 -> 18.9 mm, vias 0 -> 2
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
